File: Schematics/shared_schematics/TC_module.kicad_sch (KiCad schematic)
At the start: 13 parts, among them J7 Screw_Terminal_01x02

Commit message: add requested changes for PR
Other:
- note added: "0.1uF chosen as it is large enough to shunt unwanted low-frequency noise but small enough so that it won't distort or slow the TC's true signal the 0805 package chosen to avoid DC bias aging due to physically larger dielectric layers"
- note added: "1 nF chosen in the 0603 package due to its higher self-resonant-frequnecy, allowing it to filter HF noise coming from TC leads. the smaller 0603 package also has a lower ESL which shifts the SRF higher"
- note added: "common-mode decoupling to reduce high-frequency interference on both lines."
- note added: "decoupling for low-frequency differential-mode noise suppression."
- note added: "https://e2e.ti.com/cfs-file/__key/communityserver-discussions-components-files/73/common-mode-and-differential-filter.pdf"
- note added: "place as close as possible to thermocouple input to minimize inductance and prevent noise pickup"
- note added: "resource for decoupling circuit"
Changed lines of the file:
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@@
+		)
+	)
+	(text "common-mode decoupling to reduce \nhigh-frequency interference on both lines."
+		(exclude_from_sim no)
+		(at 248.412 92.71 0)
+		(effects
+			(font
+				(size 1.27 1.27)
+				(thickness 0.254)
+				(bold yes)
+				(color 0 0 0 1)
+			)
+		)
+	)
+	(text "0.1uF chosen as it is large enough to shunt unwanted\nlow-frequency noise but small enough so that it won't distort\nor slow the TC's true signal\n\nthe 0805 package chosen to avoid DC bias aging due \nto physically larger dielectric layers"
+		(exclude_from_sim no)
+		(at 248.412 80.01 0)
+		(effects
+			(font
+				(size 1.27 1.27)
+				(color 0 0 0 1)
+			)
+		)
+	)
+	(text "decoupling for low-frequency \ndifferential-mode noise suppression. "
+		(exclude_from_sim no)
+		(at 247.65 70.104 0)
+		(effects
+			(font
+				(size 1.27 1.27)
+				(thickness 0.254)
+				(bold yes)
+				(color 0 0 0 1)
+			)
+		)
+	)
+	(text "place as close as possible to thermocouple input\nto minimize inductance and prevent noise pickup"
+		(exclude_from_sim no)
+		(at 218.694 56.388 0)
+		(effects
+			(font
+				(size 1.27 1.27)
+				(color 0 0 0 1)
+			)
+		)
+	)
+	(text "resource for decoupling circuit"
+		(exclude_from_sim no)
+		(at 169.164 129.794 0)
+		(effects
+			(font
+				(size 1.27 1.27)
+				(color 0 0 0 1)
+			)
+		)
+	)
+	(text "1 nF chosen in the 0603 package due to its higher\nself-resonant-frequnecy, allowing it to filter\nHF noise coming from TC leads.\n\nthe smaller 0603 package also has a lower ESL \nwhich shifts the SRF higher"
+		(exclude_from_sim no)
+		(at 249.174 103.378 0)
+		(effects
+			(font
+				(size 1.27 1.27)
+				(color 0 0 0 1)
+			)
+		)
+	)
+	(text "https://e2e.ti.com/cfs-file/__key/communityserver-discussions-components-files/73/common-mode-and-differential-filter.pdf"
+		(exclude_from_sim no)
+		(at 217.932 132.842 0)
+		(effects
+			(font
+				(size 1.27 1.27)
+			)
+			(href "https://e2e.ti.com/cfs-file/__key/communityserver-discussions-components-files/73/common-mode-and-differential-filter.pdf")
 		)
 	)
@@
 		)
 	)
+	(sheet_instances
+		(path "/"
+			(page "1")
+		)
+	)

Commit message: add all circuitry and missing datasheets
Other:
- moved on the sheet: C30, C31, C32, D18A, D18B, J7, R24, R25, R26, R27, R28, R29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

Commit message: layout work
#TODO
- smaller 3V3 buck, add HF cap
- finish layout
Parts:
- TH1: footprint Resistor_SMD:R_0603_1608Metric_Pad0.98x0.95mm_HandSolder -> Resistor_SMD:R_0402_1005Metric
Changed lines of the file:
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@@
 			)
 		)
-		(property "Footprint" "Resistor_SMD:R_0603_1608Metric_Pad0.98x0.95mm_HandSolder"
+		(property "Footprint" "Resistor_SMD:R_0402_1005Metric"
 			(at 74.93 95.25 0)
 			(effects

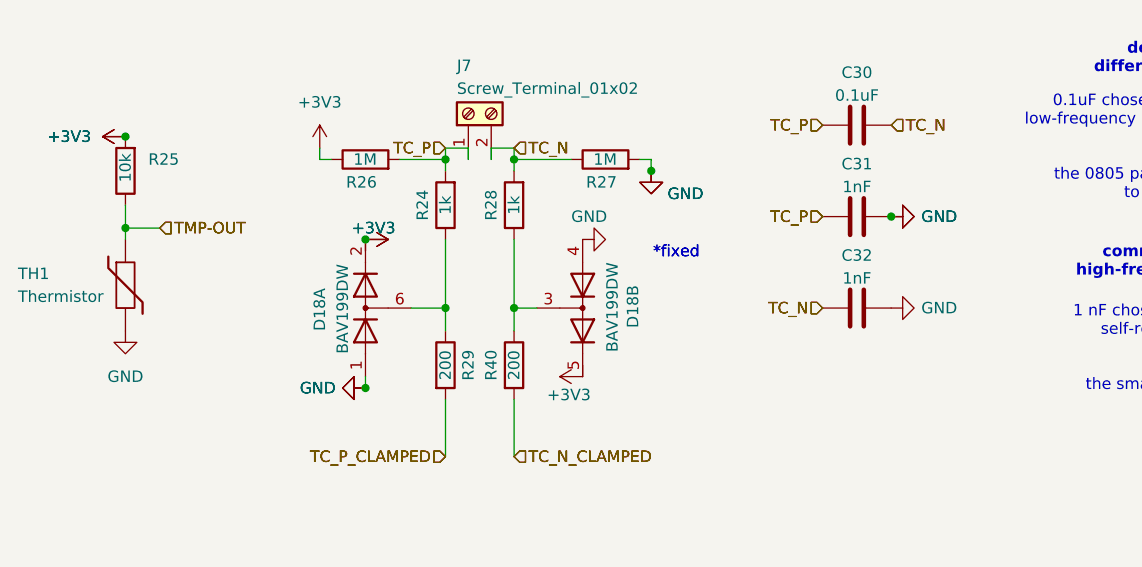
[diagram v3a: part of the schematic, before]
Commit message: finish layout
- model paths need to be fixed
- waiting for confirmation for shared folders
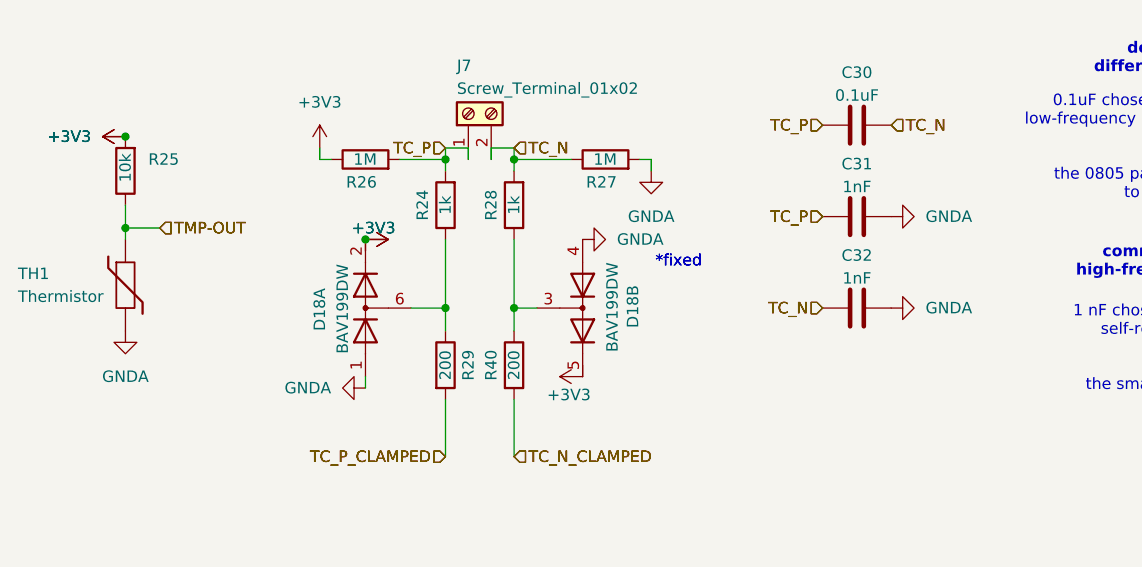
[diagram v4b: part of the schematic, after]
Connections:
- net GND renamed GNDA

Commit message: organizational work
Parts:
- C30: JLCPCB (none) -> C49678
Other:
- note added: "place as close as possible to thermocouple input for CJC measuring accuracy"
- note removed: "0.1uF chosen as it is large enough to shunt unwanted low-frequency noise but small enough so that it won't distort or slow the TC's true signal the 0805 package chosen to avoid DC bias aging due to physically larger dielectric layers"
- note removed: "1 nF chosen in the 0603 package due to its higher self-resonant-frequnecy, allowing it to filter HF noise coming from TC leads. the smaller 0603 package also has a lower ESL which shifts the SRF higher"
- note removed: "common-mode decoupling to reduce high-frequency interference on both lines."
- note removed: "decoupling for low-frequency differential-mode noise suppression."
- note removed: "https://e2e.ti.com/cfs-file/__key/communityserver-discussions-components-files/73/common-mode-and-differential-filter.pdf"
- note removed: "resource for decoupling circuit"
- moved on the sheet: C30, C31, C32, D18A, D18B, J7, R24, R25, R26, R27, R28, R29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

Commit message: routing work
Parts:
- removed R25: 10k, Resistor_SMD:R_0603_1608Metric, symbol Device:R
- removed TH1: Thermistor, Resistor_SMD:R_0402_1005Metric, symbol Device:Thermistor
- renumbered C30 to C53, C31 to C54, C32 to C55, D18 to D9, J7 to J11, R26 to R54, R24 to R55, R29 to R56, R28 to R57, R40 to R58, R27 to R59
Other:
- note removed: "place as close as possible to thermocouple input for CJC measuring accuracy"

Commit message: more routing work
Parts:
- renumbered C53 to C30, C54 to C31, C55 to C32, D9 to D18, J11 to J7, R55 to R24, R54 to R26, R59 to R27, R57 to R28, R56 to R29, R58 to R40
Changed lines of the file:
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@@
 		(on_board yes)
 		(dnp no)
-		(property "Reference" "#PWR0103"
+		(property "Reference" "#PWR0118"
 			(at 135.89 90.17 0)
 			(effects
@@
 		(on_board yes)
 		(dnp no)
-		(property "Reference" "R54"
+		(property "Reference" "R26"
 			(at 140.97 83.82 90)
 			(effects
@@
 		(on_board yes)
 		(dnp no)
-		(property "Reference" "R55"
+		(property "Reference" "R24"
 			(at 146.05 86.36 90)
 			(effects
@@
 		(on_board yes)
 		(dnp no)
-		(property "Reference" "C55"
+		(property "Reference" "C32"
 			(at 194.31 91.948 90)
 			(effects
@@
 		(on_board yes)
 		(dnp no)
-		(property "Reference" "R59"
+		(property "Reference" "R27"
 			(at 167.64 83.82 90)
 			(effects
@@
 		(on_board yes)
 		(dnp no)
-		(property "Reference" "C54"
+		(property "Reference" "C31"
 			(at 194.31 81.788 90)
 			(effects
@@
 		(on_board yes)
 		(dnp no)
-		(property "Reference" "R58"
+		(property "Reference" "R40"
 			(at 153.67 104.14 90)
 			(effects
@@
 		(on_board yes)
 		(dnp no)
-		(property "Reference" "D9"
+		(property "Reference" "D18"
 			(at 169.418 95.25 0)
 			(effects
@@
 		(on_board yes)
 		(dnp no)
-		(property "Reference" "D9"
+		(property "Reference" "D18"
 			(at 134.62 100.33 0)
 			(effects
@@
 		(on_board yes)
 		(dnp no)
-		(property "Reference" "#PWR0138"
+		(property "Reference" "#PWR0114"
 			(at 167.64 105.41 0)
 			(effects
@@
 		(on_board yes)
 		(dnp no)
-		(property "Reference" "R56"
+		(property "Reference" "R29"
 			(at 151.13 104.14 90)
 			(effects
@@
 		(on_board yes)
 		(dnp no)
-		(property "Reference" "#PWR0100"
+		(property "Reference" "#PWR0120"
 			(at 134.62 83.82 0)
 			(effects
@@
 		(on_board yes)
 		(dnp no)
-		(property "Reference" "R57"
+		(property "Reference" "R28"
 			(at 153.67 86.36 90)
 			(effects
@@
 		(on_board yes)
 		(dnp no)
-		(property "Reference" "C53"
+		(property "Reference" "C30"
 			(at 194.31 71.628 90)
 			(effects
@@
 		(on_board yes)
 		(dnp no)
-		(property "Reference" "J11"
+		(property "Reference" "J7"
 			(at 149.86 70.866 90)
 			(effects
@@
 		(on_board yes)
 		(dnp no)
-		(property "Reference" "#PWR0107"
+		(property "Reference" "#PWR0129"
 			(at 135.89 90.17 0)
 			(effects
